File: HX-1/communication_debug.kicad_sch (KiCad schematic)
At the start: 16 parts, among them J1 USB_C_Receptacle_USB2.0_16P, U2 USBLC6-2SC6

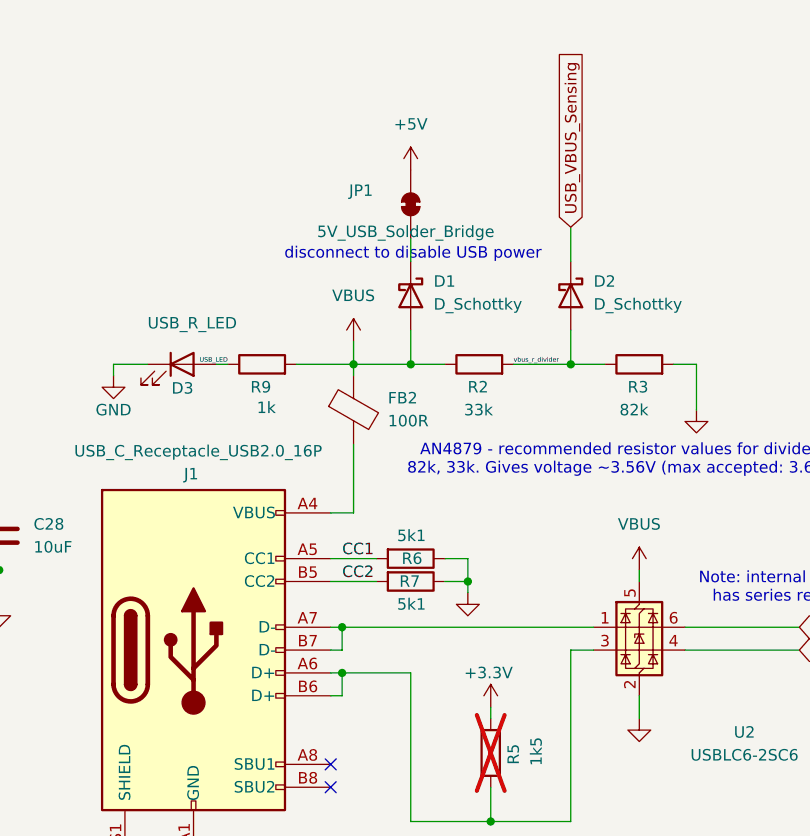
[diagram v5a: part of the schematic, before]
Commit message: add buzzer, remove one ADC diff pair
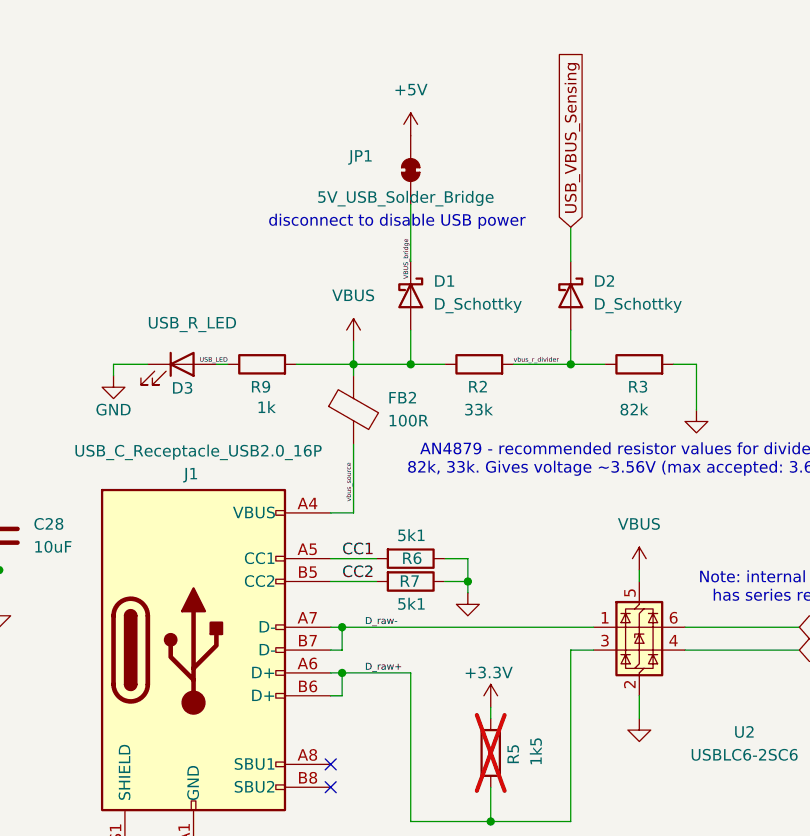
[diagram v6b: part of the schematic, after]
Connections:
- net vbus_source: now reaches FB2.2, J1.A4 (VBUS), J1.A9 (VBUS), J1.B4 (VBUS), J1.B9 (VBUS)
- net VBUS_bridge: now reaches D1.1 (K), JP1.1 (A)
- net D_raw+: now reaches J1.A6 (D+), J1.B6 (D+), R5.1, U2.3 (I/O2)
- net D_raw-: now reaches J1.A7 (D-), J1.B7 (D-), U2.1 (I/O1)
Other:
- moved on the sheet: JP1
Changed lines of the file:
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@@
 	(wire
 		(pts
-			(xy 149.86 60.96) (xy 149.86 63.5)
+			(xy 149.86 57.15) (xy 149.86 63.5)
 		)
 		(stroke
@@
 	(text "disconnect to disable USB power"
 		(exclude_from_sim no)
-		(at 150.114 62.738 0)
+		(at 148.336 59.182 0)
 		(effects
 			(font
@@
 		)
 	)
+	(label "vbus_source"
+		(at 143.51 90.17 90)
+		(effects
+			(font
+				(size 0.508 0.508)
+			)
+			(justify left bottom)
+		)
+	)
+	(label "VBUS_bridge"
+		(at 149.86 60.96 270)
+		(effects
+			(font
+				(size 0.508 0.508)
+			)
+			(justify right bottom)
+		)
+	)
 	(label "USB_LED"
 		(at 129.54 74.93 180)
@@
 			(font
 				(size 1.27 1.27)
+			)
+			(justify left bottom)
+		)
+	)
+	(label "D_raw-"
+		(at 144.78 104.14 0)
+		(effects
+			(font
+				(size 0.762 0.762)
+			)
+			(justify left bottom)
+		)
+	)
+	(label "D_raw+"
+		(at 144.78 109.22 0)
+		(effects
+			(font
+				(size 0.762 0.762)
 			)
 			(justify left bottom)
@@
 	(symbol
 		(lib_id "Jumper:SolderJumper_2_Bridged")
-		(at 149.86 57.15 90)
+		(at 149.86 53.34 90)
 		(unit 1)
 		(exclude_from_sim yes)
@@
 		(dnp no)
 		(property "Reference" "JP1"
-			(at 143.002 55.626 90)
+			(at 143.002 51.816 90)
 			(effects
 				(font
@@
 		)
 		(property "Value" "5V_USB_Solder_Bridge"
-			(at 139.446 60.198 90)
+			(at 139.446 56.388 90)
 			(effects
 				(font
@@
 		)
 		(property "Footprint" "Jumper:SolderJumper-2_P1.3mm_Bridged_RoundedPad1.0x1.5mm"
-			(at 149.86 57.15 0)
+			(at 149.86 53.34 0)
 			(effects
 				(font
@@
 		)
 		(property "Datasheet" "~"
-			(at 149.86 57.15 0)
+			(at 149.86 53.34 0)
 			(effects
 				(font
@@
 		)
 		(property "Description" "Solder Jumper, 2-pole, closed/bridged"
-			(at 149.86 57.15 0)
+			(at 149.86 53.34 0)
 			(effects
 				(font
@@
 	(symbol
 		(lib_id "power:+5V")
-		(at 149.86 53.34 0)
+		(at 149.86 49.53 0)
 		(unit 1)
 		(exclude_from_sim no)
@@
 		(fields_autoplaced yes)
 		(property "Reference" "#PWR19"
-			(at 149.86 57.15 0)
+			(at 149.86 53.34 0)
 			(effects
 				(font
@@
 		)
 		(property "Value" "+5V"
-			(at 149.86 48.26 0)
+			(at 149.86 44.45 0)
 			(effects
 				(font
@@
 		)
 		(property "Footprint" ""
-			(at 149.86 53.34 0)
+			(at 149.86 49.53 0)
 			(effects
 				(font
@@
 		)
 		(property "Datasheet" ""
-			(at 149.86 53.34 0)
+			(at 149.86 49.53 0)
 			(effects
 				(font
@@
 		)
 		(property "Description" "Power symbol creates a global label with name \"+5V\""
-			(at 149.86 53.34 0)
-			(effects
-				(font
+			(at 149.86 49.53 0)
+			(effects
+				(font

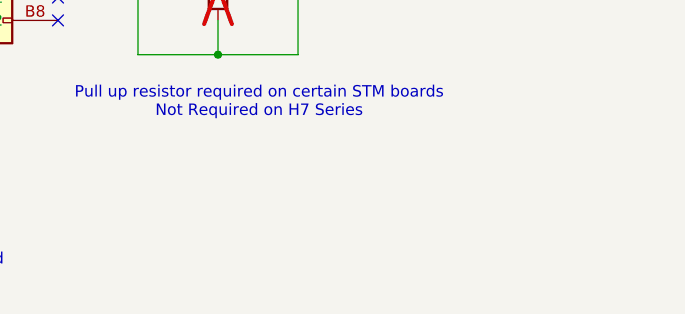
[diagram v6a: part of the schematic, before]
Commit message: remove uart7, spi2 and extra CS. Not needed. Start mapping GPIO
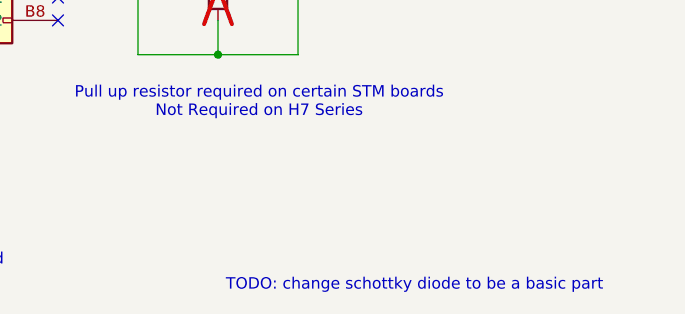
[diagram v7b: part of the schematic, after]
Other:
- note added: "TODO: change schottky diode to be a basic part"
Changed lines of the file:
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@@
+		)
+	)
+	(text "TODO: change schottky diode to be a basic part"
+		(exclude_from_sim no)
+		(at 180.594 151.384 0)
+		(effects
+			(font
+				(size 1.27 1.27)
+			)
 		)
 	)

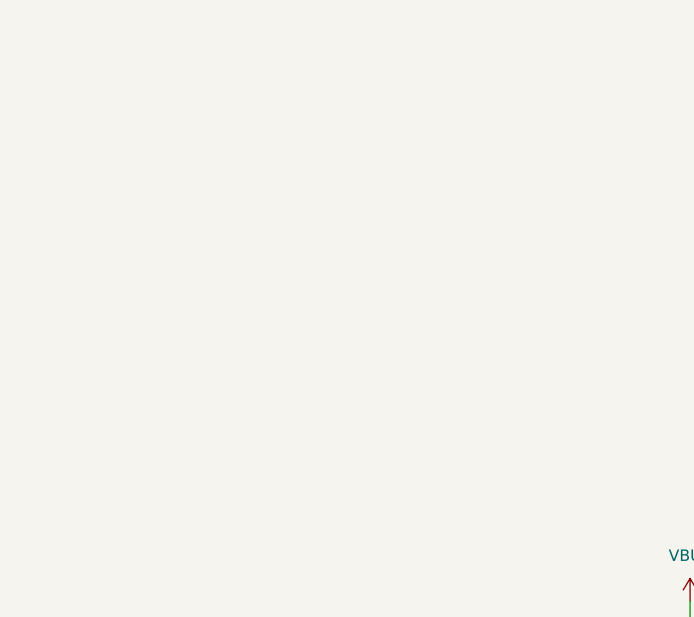
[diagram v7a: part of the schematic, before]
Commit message: add jst connectors to comms, add imu, start structuring pcb
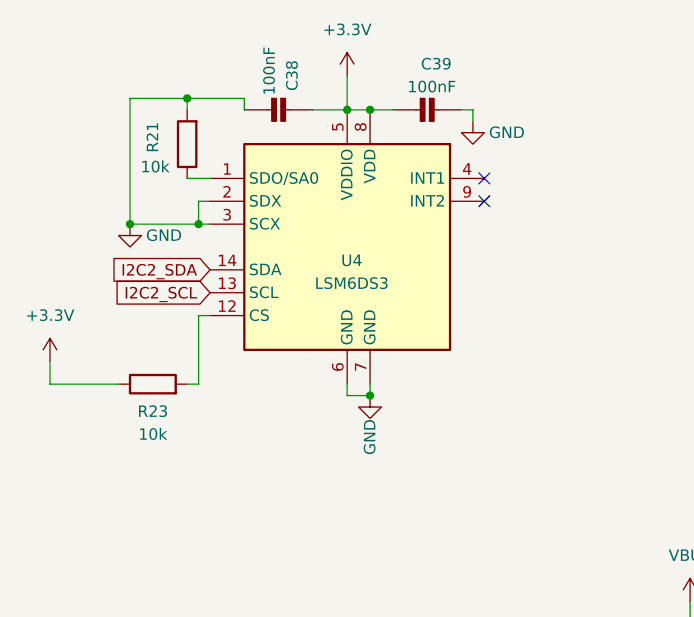
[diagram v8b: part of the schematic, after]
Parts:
- added C38, C39: 100nF, Capacitor_SMD:C_0603_1608Metric, symbol MPL3115A2_v0.2-eagle-import:CAP_CERAMIC0805-NOOUTLINE
- added R21, R23: 10k, Resistor_SMD:R_0603_1608Metric, symbol Device:R
- added U4: LSM6DS3, Package_LGA:LGA-14_3x2.5mm_P0.5mm_LayoutBorder3x4y, symbol Sensor_Motion:LSM6DS3
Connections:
- net +3.3V: now also C38.1, C39.2, R23.1, U4.5 (VDDIO), U4.8 (VDD)
- net GND: now also C38.2, C39.1, R21.2, U4.2 (SDX), U4.3 (SCX), U4.6 (GND), U4.7 (GND)
- new net: R23.2, U4.12 (CS)
- new net: R21.1, U4.1 (SDO/SA0)
- new net I2C2_SCL: U4.13 (SCL)
- new net I2C2_SDA: U4.14 (SDA)
- no-connect marks 2 -> 4
